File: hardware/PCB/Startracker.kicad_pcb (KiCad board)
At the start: 4 copper layers, 99.8 x 99.8 mm, 122 parts, among them J1 IMU_EXT, J10 Conn_01x04_Socket, J2 GPS, J3 Motor1, J4 Motor2, J5 Motor3, J6 6V, J7 SJ-3523-SMT-TR, J8 USB_C_Receptacle_USB2.0_16P, J9 Conn_01x05_Socket, Q1 2N3904, Q2 2N3904, SW1 RST, SW2 BOOT, SW3 PWR, U1 ESP32-S3-WROOM-1, U10 SX1261IMLTRT, U11 BGS12P2L6E6327XT, U12 SRV05-4, U13 TPS54308, U14 TPS2121RUXR, U2 TMC2209-LA, U3 TB6612FNG, U4 TB6612FNG, U5 PCF8574T, U7 BME280, U8 INA219BxDCN, U9 INA219BxDCN, Y2 32.00 MHz

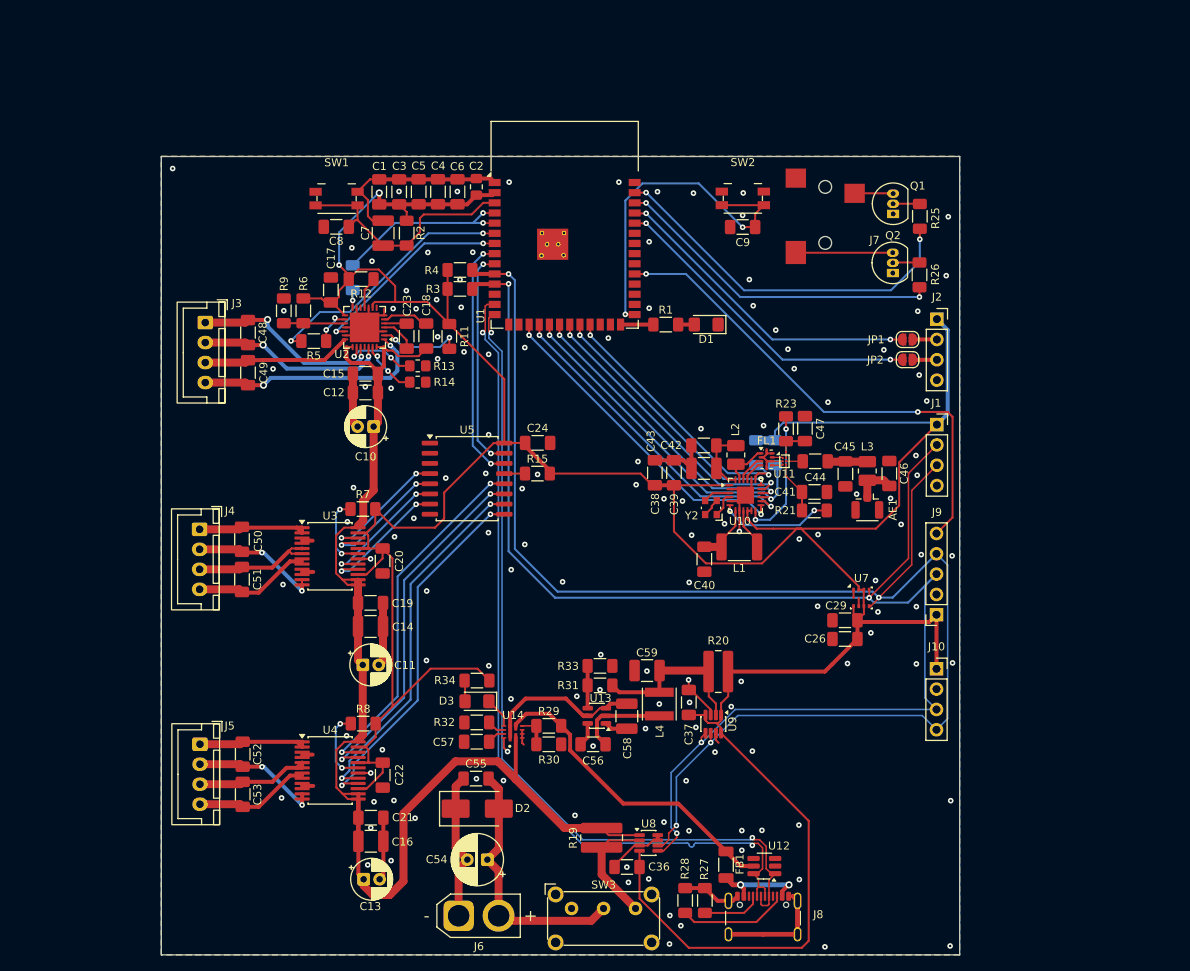
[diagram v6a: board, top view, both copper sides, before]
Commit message: Removed polar azimuth motor driver from pcb
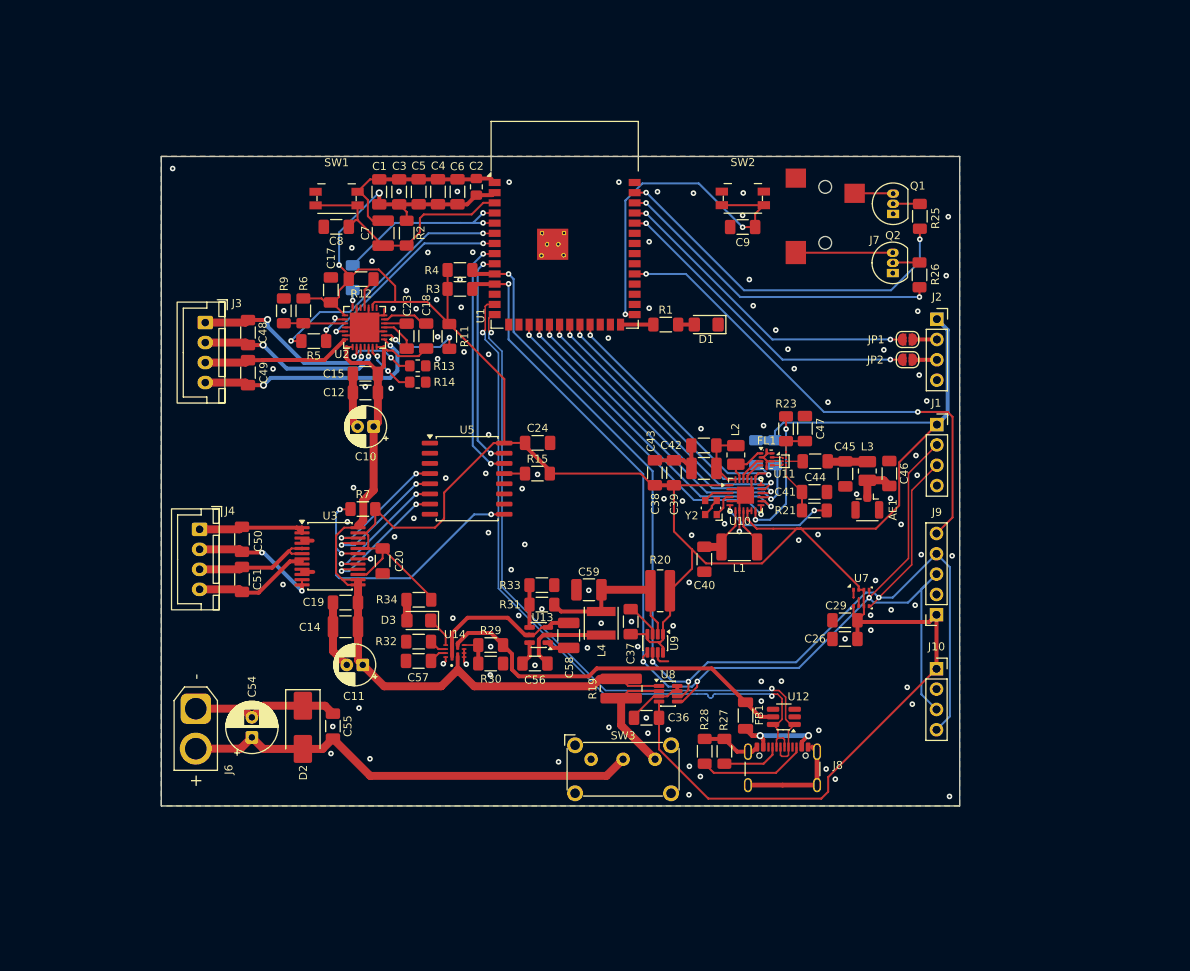
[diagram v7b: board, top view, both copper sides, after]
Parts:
- removed C13: 100u, Capacitor_THT:CP_Radial_D5.0mm_P2.00mm
- removed C16: 10u, Capacitor_SMD:C_1210_3225Metric_Pad1.33x2.70mm_HandSolder
- removed C21, C22, C52, C53: 100n, Capacitor_SMD:C_1206_3216Metric_Pad1.33x1.80mm_HandSolder
- removed J5: Motor3, Connector_JST:JST_XH_B4B-XH-A_1x04_P2.50mm_Vertical
- removed R8: 10k, Resistor_SMD:R_1206_3216Metric_Pad1.30x1.75mm_HandSolder
- removed U4: TB6612FNG, Package_SO:SSOP-24_5.3x8.2mm_P0.65mm
- moved J6 41.8 mm to (95.5, 118.1), turned to -90 degrees
- moved C54 33.2 mm to (102.5, 121.7), turned to 90 degrees
- moved D2 24.1 mm to (108.9, 120.4), turned to -90 degrees
- moved C55 19.1 mm to (112.6, 120.3), turned to -90 degrees
- moved FB1 18.8 mm to (164.2, 119.0)
- moved J8 18.8 mm to (168.8, 126.6)
- moved C36 18.8 mm to (151.8, 119.3)
- moved R19 18.8 mm to (148.7, 115.6)
- moved R27 18.8 mm to (161.6, 123.4)
- moved R28 18.8 mm to (159.1, 123.4)
- moved SW3 18.8 mm to (144.9, 124.4)
- moved U12 18.8 mm to (169.0, 119.1)
- moved U8 18.8 mm to (154.5, 116.2)
- moved C37 12.4 mm to (149.9, 107.2)
- moved D3 12.4 mm to (123.4, 107.1)
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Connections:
- R7 pad 1: Net-(U3-STBY) -> D2_STBY
- SW3 pad : (no net) -> GND
- U3 pad 19: Net-(U3-STBY) -> D2_STBY
- U5 pad 10: D3_B1 -> unconnected-(U5-P5-Pad10)
- U5 pad 11: D3_A1 -> unconnected-(U5-P6-Pad11)
- U5 pad 12: D3_A2 -> unconnected-(U5-P7-Pad12)
- U5 pad 9: D3_B2 -> D2_STBY
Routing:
- net +3.3V: track 439.8 -> 374.7 mm
- net VM: track 163.8 -> 109.8 mm
- net D3_B1: track 45.7 -> 0.00 mm, vias 2 -> 0
- net D3_B2: track 45.5 -> 0.00 mm, vias 2 -> 0
- net D3_A2: track 45.2 -> 0.00 mm, vias 2 -> 0
- net D3_A1: track 44.8 -> 0.00 mm, vias 2 -> 0
- net D2_STBY: track 0.00 -> 38.0 mm, vias 0 -> 3
- net /OBC/I2C_SCL: track 186.9 -> 150.7 mm
- net /OBC/I2C_SDA: track 188.9 -> 152.9 mm
- net Net-(D2-A2): track 32.9 -> 58.8 mm
- net /CONN/M3_A1: track 21.4 -> 0.00 mm
- net /OBC/USB_D+: track 105.3 -> 87.4 mm
- net /OBC/USB_D-: track 106.3 -> 88.5 mm
- net /CONN/M3_B1: track 16.3 -> 0.00 mm, vias 2 -> 0
- net /CONN/M3_A2: track 15.2 -> 0.00 mm
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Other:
- board size 99.8 x 99.8 mm -> 99.8 x 81.2 mm
